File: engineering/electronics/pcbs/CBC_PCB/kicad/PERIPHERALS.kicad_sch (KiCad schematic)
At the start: 7 parts, among them J2 B08B-JWPF-SK-R

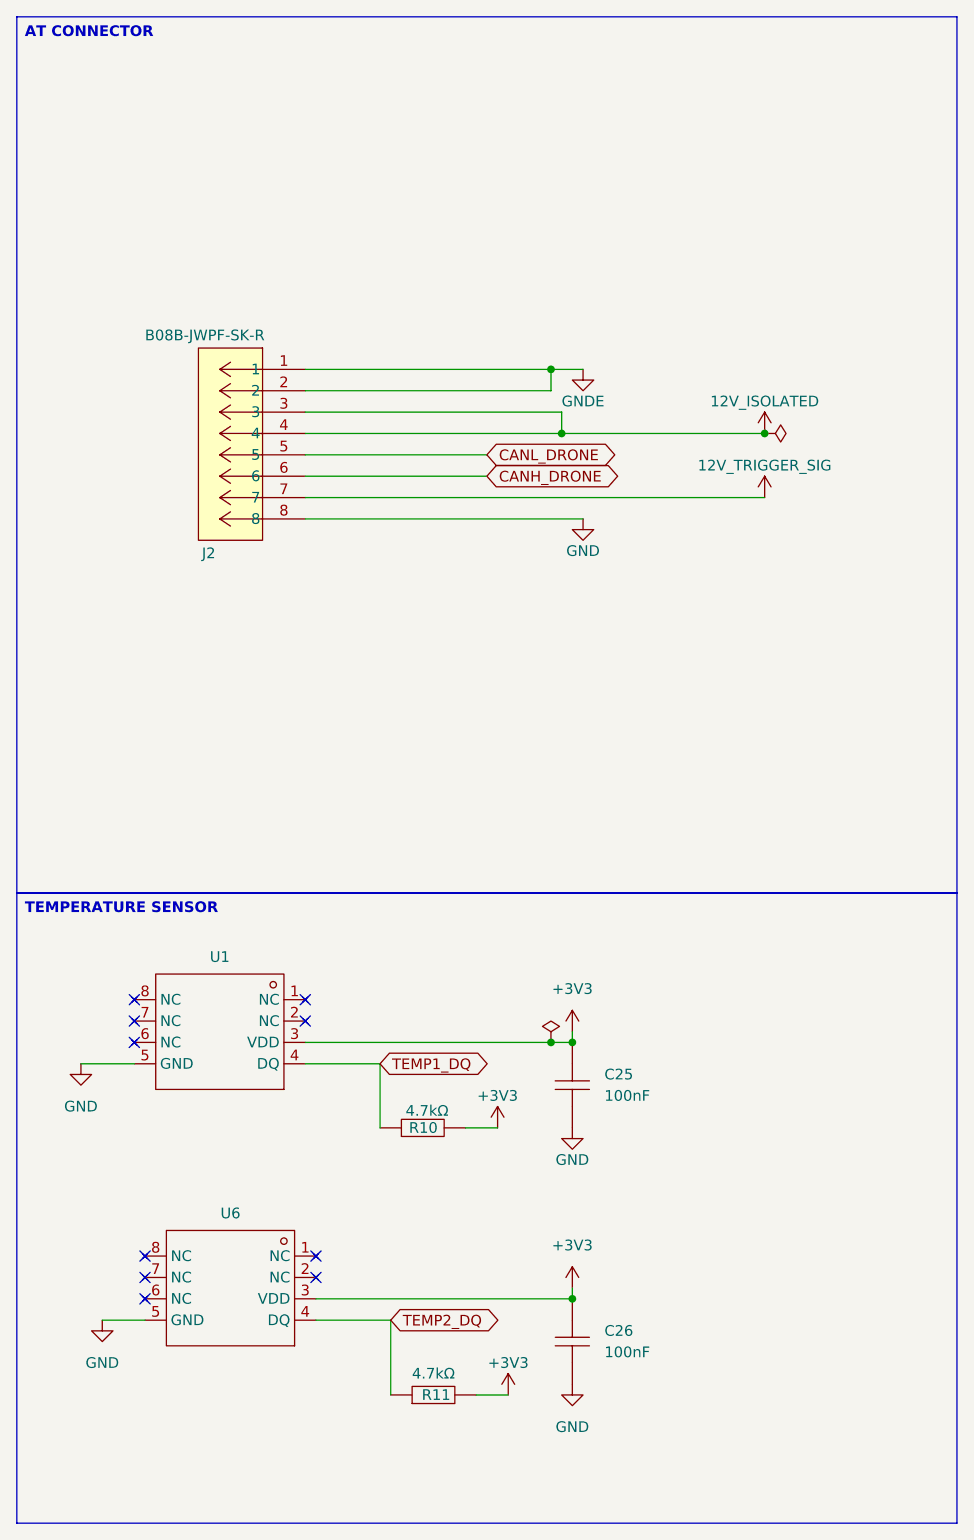
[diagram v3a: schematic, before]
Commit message: fix(cbc): integrate ordered PCB update
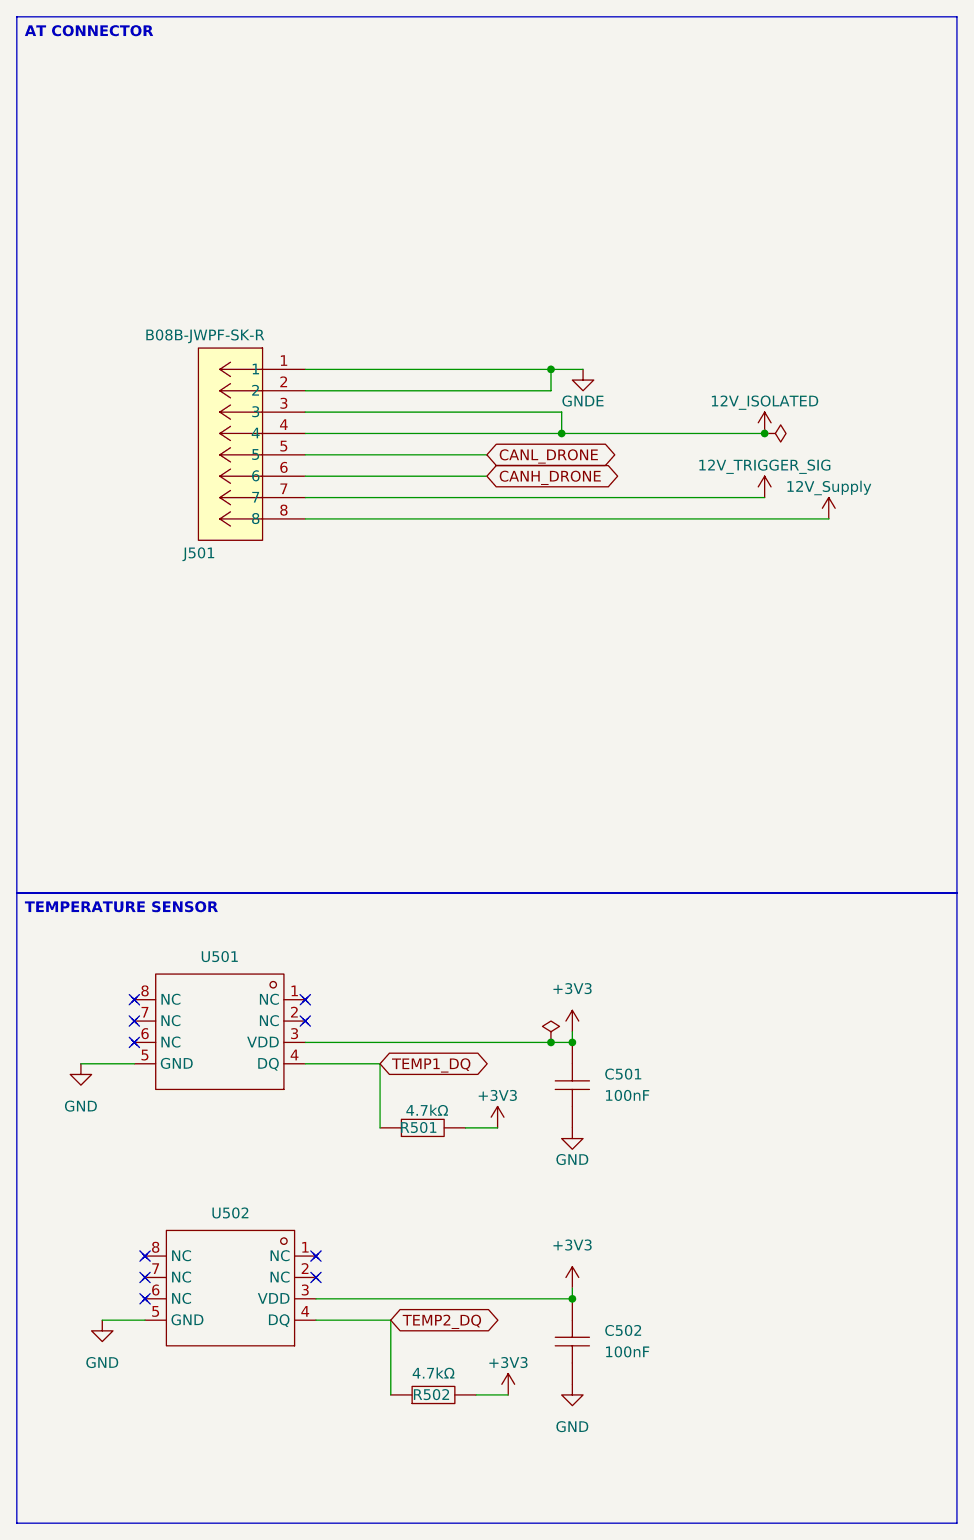
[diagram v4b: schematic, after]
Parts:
- renumbered C25 to C501, C26 to C502, J2 to J501, R10 to R501, R11 to R502, U1 to U501, U6 to U502
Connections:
- net GND: no longer J501.8
- new net 12V_Supply: J501.8
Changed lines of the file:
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@@
 	(wire
 		(pts
-			(xy 46.99 73.66) (xy 80.01 73.66)
+			(xy 46.99 73.66) (xy 109.22 73.66)
 		)
 		(stroke
@@
 		(in_pos_files yes)
 		(dnp no)
-		(property "Reference" "#PWR0158"
+		(property "Reference" "#PWR0512"
 			(at 101.6 74.93 0)
 			(hide yes)
@@
 			(project "CBC_PCB"
 				(path "/d195d1ee-585b-4211-912f-f5dd5687bc63/b4c95d27-7981-477f-a8ef-d2ce83f3675e"
-					(reference "#PWR0158")
+					(reference "#PWR0512")
 					(unit 1)
 				)
@@
 		(dnp no)
 		(fields_autoplaced yes)
-		(property "Reference" "C26"
+		(property "Reference" "C502"
 			(at 82.55 170.18 90)
 			(show_name no)
@@
 			(project "CBC_PCB"
 				(path "/d195d1ee-585b-4211-912f-f5dd5687bc63/b4c95d27-7981-477f-a8ef-d2ce83f3675e"
-					(reference "C26")
+					(reference "C502")
 					(unit 1)
 				)
@@
 		(dnp no)
 		(fields_autoplaced yes)
-		(property "Reference" "#PWR0185"
+		(property "Reference" "#PWR0501"
 			(at 20.32 144.78 0)
 			(hide yes)
@@
 			(project "CBC_PCB"
 				(path "/d195d1ee-585b-4211-912f-f5dd5687bc63/b4c95d27-7981-477f-a8ef-d2ce83f3675e"
-					(reference "#PWR0185")
+					(reference "#PWR0501")
 					(unit 1)
 				)
@@
 		(in_pos_files yes)
 		(dnp no)
-		(property "Reference" "U6"
+		(property "Reference" "U502"
 			(at 38.1 156.21 0)
 			(show_name no)
@@
 			(project "CBC_PCB"
 				(path "/d195d1ee-585b-4211-912f-f5dd5687bc63/b4c95d27-7981-477f-a8ef-d2ce83f3675e"
-					(reference "U6")
+					(reference "U502")
 					(unit 1)
 				)
@@
 		(dnp no)
 		(fields_autoplaced yes)
-		(property "Reference" "#PWR0184"
+		(property "Reference" "#PWR0502"
 			(at 22.86 175.26 0)
 			(hide yes)
@@
 			(project "CBC_PCB"
 				(path "/d195d1ee-585b-4211-912f-f5dd5687bc63/b4c95d27-7981-477f-a8ef-d2ce83f3675e"
-					(reference "#PWR0184")
+					(reference "#PWR0502")
 					(unit 1)
 				)
@@
 		(in_pos_files yes)
 		(dnp no)
-		(property "Reference" "#PWR069"
+		(property "Reference" "#PWR0503"
 			(at 69.85 149.86 0)
 			(hide yes)
@@
 			(project "CBC_PCB"
 				(path "/d195d1ee-585b-4211-912f-f5dd5687bc63/b4c95d27-7981-477f-a8ef-d2ce83f3675e"
-					(reference "#PWR069")
+					(reference "#PWR0503")
+					(unit 1)
+				)
+			)
+		)
+	)
+	(symbol
+		(lib_id "power:+5V")
+		(at 109.22 73.66 0)
+		(unit 1)
+		(body_style 1)
+		(exclude_from_sim no)
+		(in_bom yes)
+		(on_board yes)
+		(in_pos_files yes)
+		(dnp no)
+		(property "Reference" "#PWR0510"
+			(at 109.22 77.47 0)
+			(hide yes)
+			(show_name no)
+			(do_not_autoplace no)
+			(effects
+				(font
+					(size 1.27 1.27)
+				)
+			)
+		)
+		(property "Value" "12V_Supply"
+			(at 109.22 69.85 0)
+			(show_name no)
+			(do_not_autoplace no)
+			(effects
+				(font
+					(size 1.27 1.27)
+				)
+			)
+		)
+		(property "Footprint" ""
+			(at 109.22 73.66 0)
+			(hide yes)
+			(show_name no)
+			(do_not_autoplace no)
+			(effects
+				(font
+					(size 1.27 1.27)
+				)
+			)
+		)
+		(property "Datasheet" ""
+			(at 109.22 73.66 0)
+			(hide yes)
+			(show_name no)
+			(do_not_autoplace no)
+			(effects
+				(font
+					(size 1.27 1.27)
+				)
+			)
+		)
+		(property "Description" "Power symbol creates a global label with name \"+5V\""
+			(at 109.22 73.66 0)
+			(hide yes)
+			(show_name no)
+			(do_not_autoplace no)
+			(effects
+				(font
+					(size 1.27 1.27)
+				)
+			)
+		)
+		(pin "1"
+		)
+		(instances
+			(project "CBC_PCB"
+				(path "/d195d1ee-585b-4211-912f-f5dd5687bc63/b4c95d27-7981-477f-a8ef-d2ce83f3675e"
+					(reference "#PWR0510")
 					(unit 1)
 				)
@@
 		(in_pos_files yes)
 		(dnp no)
-		(property "Reference" "#PWR0159"
+		(property "Reference" "#PWR0509"
 			(at 80.01 62.23 0)
 			(hide yes)
@@
 			(project "CBC_PCB"
 				(path "/d195d1ee-585b-4211-912f-f5dd5687bc63/b4c95d27-7981-477f-a8ef-d2ce83f3675e"
-					(reference "#PWR0159")
+					(reference "#PWR0509")
 					(unit 1)
 				)
@@
 		(dnp no)
 		(fields_autoplaced yes)
-		(property "Reference" "#FLG051"
+		(property "Reference" "#FLG0502"
 			(at 102.87 63.5 0)
 			(hide yes)
@@
 			(project "CBC_PCB"
 				(path "/d195d1ee-585b-4211-912f-f5dd5687bc63/b4c95d27-7981-477f-a8ef-d2ce83f3675e"
-					(reference "#FLG051")
-					(unit 1)
-				)
-			)
-		)
-	)
-	(symbol
-		(lib_id "power:GND")
-		(at 80.01 73.66 0)
-		(unit 1)
-		(body_style 1)
-		(exclude_from_sim no)
-		(in_bom yes)
-		(on_board yes)
-		(in_pos_files yes)
-		(dnp no)
-		(property "Reference" "#PWR0157"
-			(at 80.01 80.01 0)
-			(hide yes)
-			(show_name no)
-			(do_not_autoplace no)
-			(effects
-				(font
-					(size 1.27 1.27)
-				)
-			)
-		)
-		(property "Value" "GND"
-			(at 80.01 77.47 0)
-			(show_name no)
-			(do_not_autoplace no)
-			(effects
-				(font
-					(size 1.27 1.27)
-				)
-			)
-		)
-		(property "Footprint" ""
-			(at 80.01 73.66 0)
-			(hide yes)
-			(show_name no)
-			(do_not_autoplace no)
-			(effects
-				(font
-					(size 1.27 1.27)
-				)
-			)
-		)
-		(property "Datasheet" ""
-			(at 80.01 73.66 0)
-			(hide yes)
-			(show_name no)
-			(do_not_autoplace no)
-			(effects
-				(font
-					(size 1.27 1.27)
-				)
-			)
-		)
-		(property "Description" "Power symbol creates a global label with name \"GND\" , ground"
-			(at 80.01 73.66 0)
-			(hide yes)
-			(show_name no)
-			(do_not_autoplace no)
-			(effects
-				(font
-					(size 1.27 1.27)
-				)
-			)
-		)
-		(pin "1"
-		)
-		(instances
-			(project "CBC_PCB"
-				(path "/d195d1ee-585b-4211-912f-f5dd5687bc63/b4c95d27-7981-477f-a8ef-d2ce83f3675e"
-					(reference "#PWR0157")
+					(reference "#FLG0502")
 					(unit 1)
 				)
@@
 		(in_pos_files yes)
 		(dnp no)
-		(property "Reference" "R10"
+		(property "Reference" "R501"
 			(at 62.738 146.05 0)
 			(show_name no)
@@
 			(project "CBC_PCB"
 				(path "/d195d1ee-585b-4211-912f-f5dd5687bc63/b4c95d27-7981-477f-a8ef-d2ce83f3675e"
-					(reference "R10")
+					(reference "R501")
 					(unit 1)
 				)
@@
 		(dnp no)
 		(fields_autoplaced yes)
-		(property "Reference" "#FLG069"
+		(property "Reference" "#FLG0501"
 			(at 76.2 134.62 0)
 			(hide yes)
@@
 			(project "CBC_PCB"
 				(path "/d195d1ee-585b-4211-912f-f5dd5687bc63/b4c95d27-7981-477f-a8ef-d2ce83f3675e"
-					(reference "#FLG069")
+					(reference "#FLG0501")
 					(unit 1)
 				)
@@
 		(dnp no)
 		(fields_autoplaced yes)
-		(property "Reference" "#PWR067"
+		(property "Reference" "#PWR0505"
 			(at 78.74 138.43 0)
 			(hide yes)
@@
 			(project "CBC_PCB"
 				(path "/d195d1ee-585b-4211-912f-f5dd5687bc63/b4c95d27-7981-477f-a8ef-d2ce83f3675e"
-					(reference "#PWR067")
+					(reference "#PWR0505")
 					(unit 1)
 				)
@@
 		(in_pos_files yes)
 		(dnp no)
-		(property "Reference" "U1"
+		(property "Reference" "U501"
 			(at 36.83 125.73 0)
 			(show_name no)
@@
 			(project "CBC_PCB"
 				(path "/d195d1ee-585b-4211-912f-f5dd5687bc63/b4c95d27-7981-477f-a8ef-d2ce83f3675e"
-					(reference "U1")
+					(reference "U501")
 					(unit 1)
 				)
@@
 		(in_pos_files yes)
 		(dnp no)
-		(property "Reference" "#PWR071"
+		(property "Reference" "#PWR0504"
 			(at 71.12 181.61 0)
 			(hide yes)
@@
 			(project "CBC_PCB"
 				(path "/d195d1ee-585b-4211-912f-f5dd5687bc63/b4c95d27-7981-477f-a8ef-d2ce83f3675e"
-					(reference "#PWR071")
+					(reference "#PWR0504")
 					(unit 1)
 				)
@@
 		(in_pos_files yes)
 		(dnp no)
-		(property "Reference" "R11"
+		(property "Reference" "R502"
 			(at 64.262 177.8 0)
 			(show_name no)
@@
 			(project "CBC_PCB"
 				(path "/d195d1ee-585b-4211-912f-f5dd5687bc63/b4c95d27-7981-477f-a8ef-d2ce83f3675e"
-					(reference "R11")
+					(reference "R502")
 					(unit 1)
 				)
@@
 		(dnp no)
 		(fields_autoplaced yes)
-		(property "Reference" "C25"
+		(property "Reference" "C501"
 			(at 82.55 139.7 90)
 			(show_name no)
@@
 			(project "CBC_PCB"
 				(path "/d195d1ee-585b-4211-912f-f5dd5687bc63/b4c95d27-7981-477f-a8ef-d2ce83f3675e"
-					(reference "C25")
+					(reference "C501")
 					(unit 1)
 				)
@@
 		(in_pos_files yes)
 		(dnp no)
-		(property "Reference" "#PWR068"
+		(property "Reference" "#PWR0506"
 			(at 78.74 152.4 0)
 			(hide yes)
@@
 			(project "CBC_PCB"
 				(path "/d195d1ee-585b-4211-912f-f5dd5687bc63/b4c95d27-7981-477f-a8ef-d2ce83f3675e"
-					(reference "#PWR068")
+					(reference "#PWR0506")
 					(unit 1)
 				)
@@
 		(dnp no)
 		(fields_autoplaced yes)
-		(property "Reference" "#PWR074"
+		(property "Reference" "#PWR0508"
 			(at 78.74 182.88 0)
 			(hide yes)
@@
 			(project "CBC_PCB"
 				(path "/d195d1ee-585b-4211-912f-f5dd5687bc63/b4c95d27-7981-477f-a8ef-d2ce83f3675e"
-					(reference "#PWR074")
+					(reference "#PWR0508")
 					(unit 1)
 				)
@@
 		(dnp no)
 		(fields_autoplaced yes)
-		(property "Reference" "#PWR073"
+		(property "Reference" "#PWR0507"
 			(at 78.74 168.91 0)
 			(hide yes)
@@
 			(project "CBC_PCB"
 				(path "/d195d1ee-585b-4211-912f-f5dd5687bc63/b4c95d27-7981-477f-a8ef-d2ce83f3675e"
-					(reference "#PWR073")
+					(reference "#PWR0507")
 					(unit 1)
 				)
@@
 		(in_pos_files yes)
 		(dnp no)
-		(property "Reference" "#PWR0156"
+		(property "Reference" "#PWR0511"
 			(at 101.6 67.31 0)
 			(hide yes)
@@
 			(project "CBC_PCB"
 				(path "/d195d1ee-585b-4211-912f-f5dd5687bc63/b4c95d27-7981-477f-a8ef-d2ce83f3675e"
-					(reference "#PWR0156")
+					(reference "#PWR0511")
 					(unit 1)
 				)
@@
 		(in_pos_files yes)
 		(dnp no)
-		(property "Reference" "J2"
+		(property "Reference" "J501"
 			(at 36.322 78.486 0)
 			(show_name no)
@@
 			(project "CBC_PCB"
 				(path "/d195d1ee-585b-4211-912f-f5dd5687bc63/b4c95d27-7981-477f-a8ef-d2ce83f3675e"
-					(reference "J2")
+					(reference "J501")
 					(unit 1)
 				)
